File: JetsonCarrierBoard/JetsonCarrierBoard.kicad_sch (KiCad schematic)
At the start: 0 parts

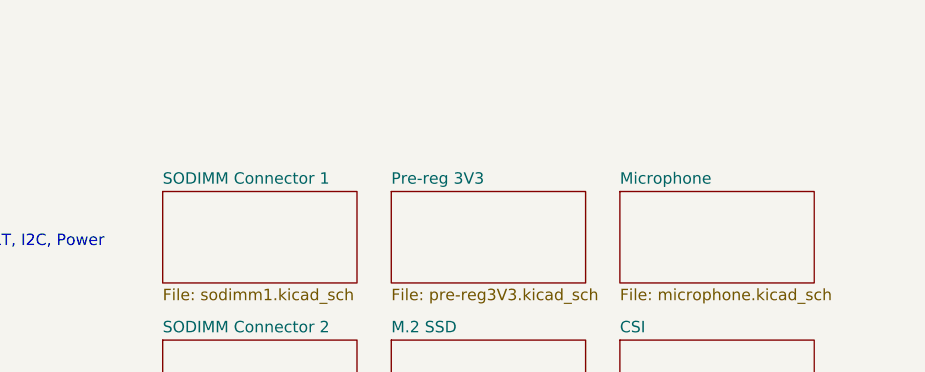
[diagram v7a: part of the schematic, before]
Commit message: Fan and Debug UART
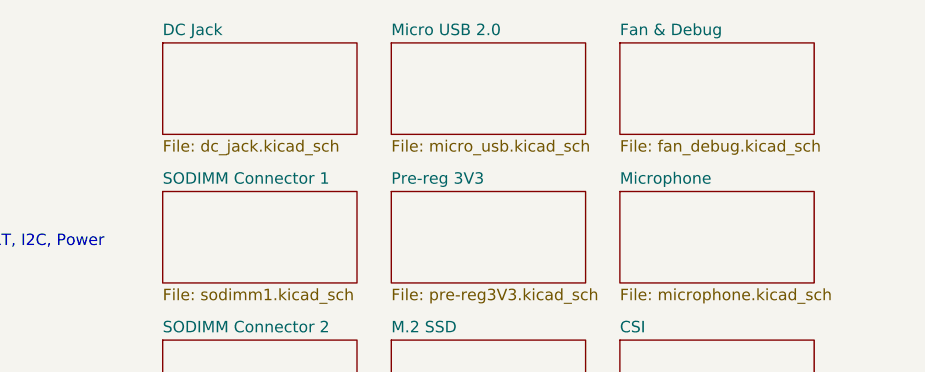
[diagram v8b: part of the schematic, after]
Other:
- added sheet DC Jack (dc_jack.kicad_sch)
- added sheet Fan & Debug (fan_debug.kicad_sch)
- added sheet Micro USB 2.0 (micro_usb.kicad_sch)
